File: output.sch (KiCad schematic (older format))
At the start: 7 parts, among them J1 5-20 V⎓, Q1 MMBT2222ALT1G, Q2 DMP4015SSS

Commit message: Corrected MOSFET connections
I had the source and drain reversed—whoops.  After fixing it with an
X-Acto knife and some point-to-point wiring, I've updated the schematic
and PCB files accordingly.

THIS ALSO MARKS THE BEGINNING OF DEVELOPMENT OF THE NEXT BOARD REVISION.
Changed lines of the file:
@@
 Title "PD Buddy"
 Date ""
-Rev "0.1"
+Rev "0.2"
 Comp ""
 Comment1 ""
@@
 F 3 "http://www.diodes.com/_files/datasheets/DMP4015SSS.pdf" H 6600 3600 50  0001 C CNN
 	1    6400 3550
-	1    0    0    -1
+	1    0    0    1
 $EndComp
 $Comp

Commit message: Corrected BJT connections
Boy, I'm good at messing up transistors!  This time it was just the pin
numbers for the collector and emitter reversed, because I didn't copy
the symbol from the datasheet but rather assumed another SMT 2222 would
have the same pinout.  Interestingly, it actually was able to control
the MOSFET at VBUS = 5 V and at VBUS = 9 V, but at VBUS = 15 V the
reversed transistor couldn't pull the MOSFET gate down enough.
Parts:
- Q1: symbol PZT2222A -> MMBT2222AL
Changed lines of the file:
@@
 $EndComp
 $Comp
-L PZT2222A Q1
+L MMBT2222AL Q1
 U 1 1 588FA577
 P 5450 4050

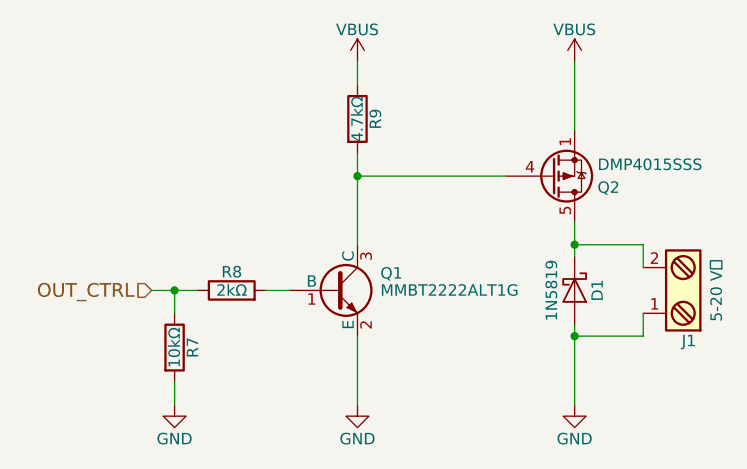
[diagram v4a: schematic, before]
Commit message: Reversed output connector, widened traces
Now there's a filled zone connecting the MOSFET output to the connector,
and the + side of the output is close to the MOSFET.  Both connector
leads have no thermal relief, for minimum resistance.
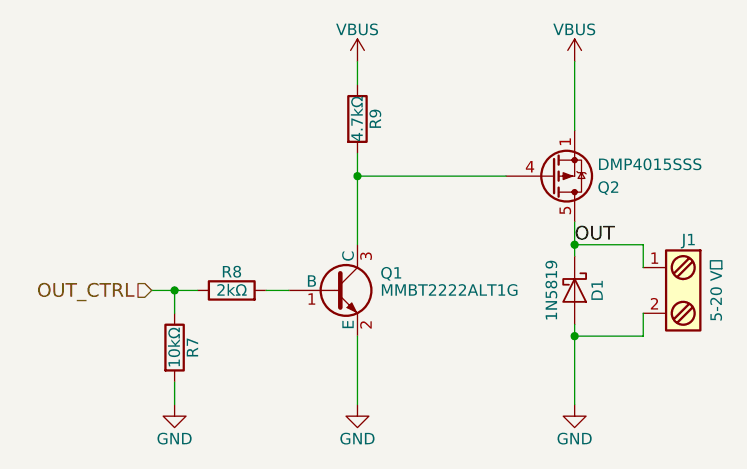
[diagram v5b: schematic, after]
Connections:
- net GND: now also J1.2; no longer J1.1
- net OUT: now reaches D1.1 (K), Q2.5 (D), Q2.6 (D), Q2.7 (D), Q2.8 (D)
- net OUT: now also J1.1; no longer J1.2
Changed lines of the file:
@@
 F 3 "" H 6975 4050 50  0001 C CNN
 	1    7000 4050
-	-1   0    0    1
+	-1   0    0    -1
 $EndComp
 Text HLabel 4650 4050 0    60   Input ~ 0
@@
 Wire Wire Line
 	4750 4550 4750 4450
+Text Label 6500 3850 0    60   ~ 0
+OUT
 $EndSCHEMATC

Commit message: SMD flyback diode, 0.5 mm shorter PCB
Since it really seems like a good idea to include the flyback diode by
default, I decided to change it to a surface mount device.  After that,
I noticed that it would be easy to shave another 0.5 mm off the end of
the PCB, so I did.
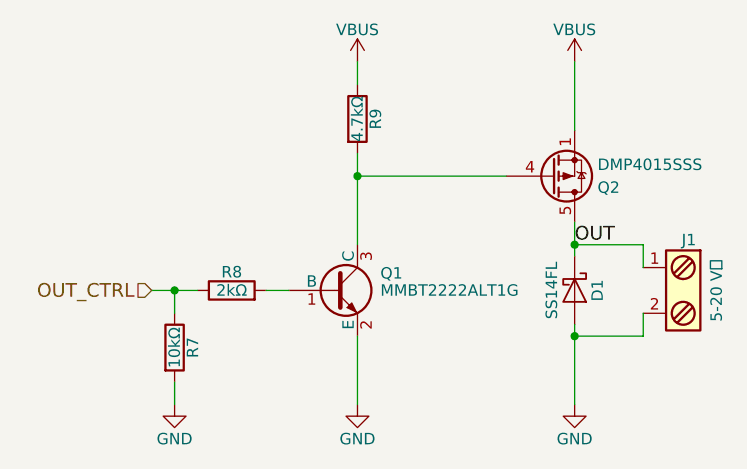
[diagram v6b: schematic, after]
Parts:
- D1: value 1N5819 -> SS14FL; footprint Diodes_THT:D_DO-41_SOD81_P2.54mm_Vertical_AnodeUp -> Diodes_SMD:D_SOD-123F
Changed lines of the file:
@@
 P 6500 4050
 F 0 "D1" H 6500 4150 50  0000 C CNN
-F 1 "1N5819" H 6500 3950 50  0000 C CNN
-F 2 "Diodes_THT:D_DO-41_SOD81_P2.54mm_Vertical_AnodeUp" H 6500 4050 50  0001 C CNN
-F 3 "" H 6500 4050 50  0000 C CNN
+F 1 "SS14FL" H 6500 3950 50  0000 C CNN
+F 2 "Diodes_SMD:D_SOD-123F" H 6500 4050 50  0001 C CNN
+F 3 "https://www.fairchildsemi.com/datasheets/SS/SS14FL.pdf" H 6500 4050 50  0001 C CNN
 	1    6500 4050
 	0    1    1    0
